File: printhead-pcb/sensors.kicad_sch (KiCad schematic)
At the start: 16 parts, among them J10 T2, J11 T3, J8 T0, J9 T1, U4 ADS1015IDGS

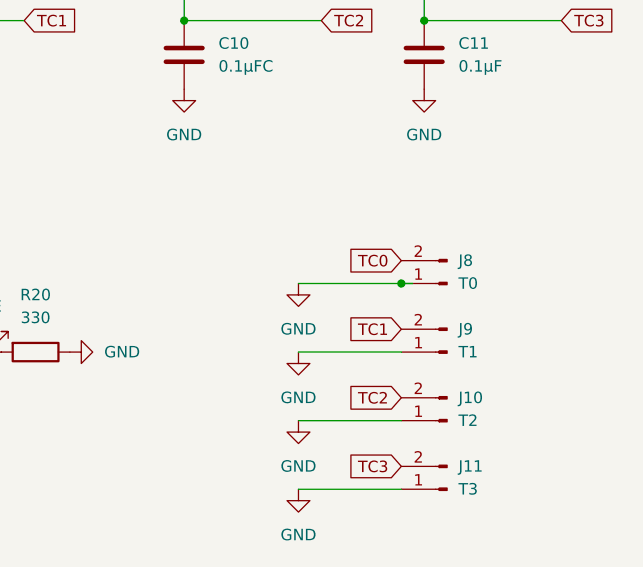
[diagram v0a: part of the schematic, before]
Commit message: removed led driver, added RJ45 (data connector), fan 3. 4. on off
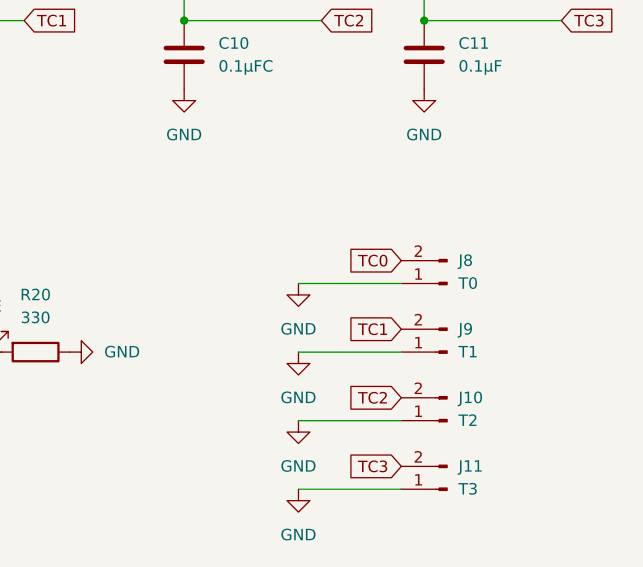
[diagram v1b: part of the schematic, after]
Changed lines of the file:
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@@
-	)
-	(junction
-		(at 176.53 125.73)
-		(diameter 0)
-		(color 0 0 0 0)
 	)
 	(junction
@@
 		(pts
 			(xy 119.38 96.52) (xy 119.38 82.55)
-		)
-		(stroke
-			(width 0)
-			(type default)
-		)
-	)
-	(wire
-		(pts
-			(xy 165.1 125.73) (xy 176.53 125.73)
 		)
 		(stroke
@@
 	(wire
 		(pts
-			(xy 177.8 125.73) (xy 176.53 125.73)
+			(xy 165.1 125.73) (xy 176.53 125.73)
 		)
 		(stroke

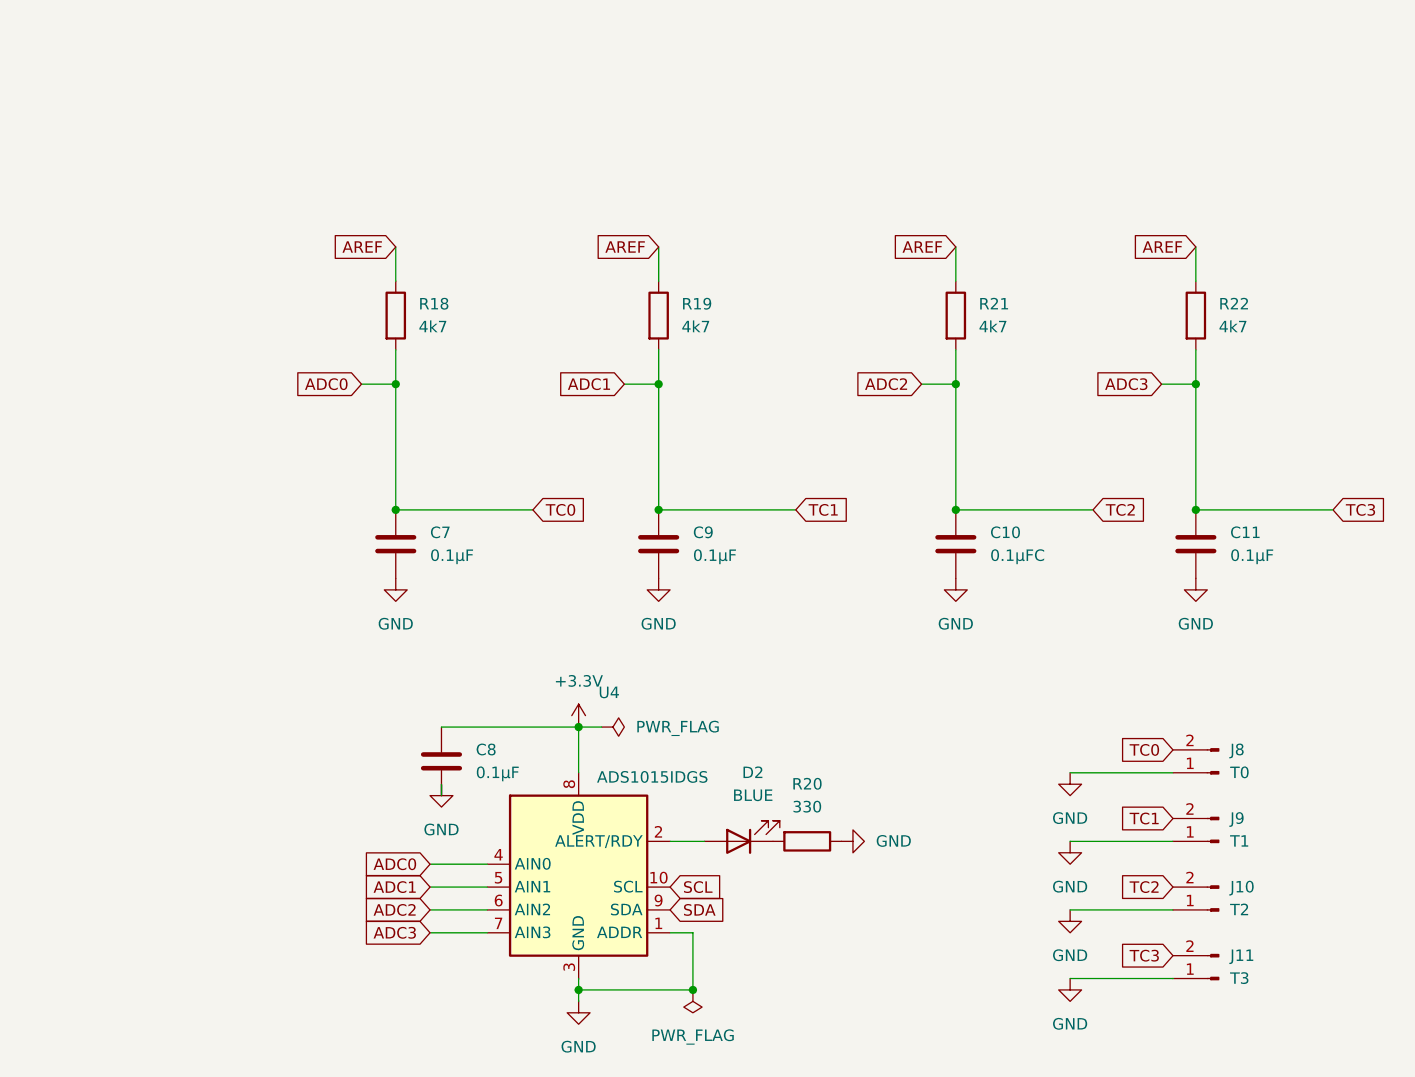
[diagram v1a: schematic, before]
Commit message: Beschriftungen im Schaltplan hinzugefügt
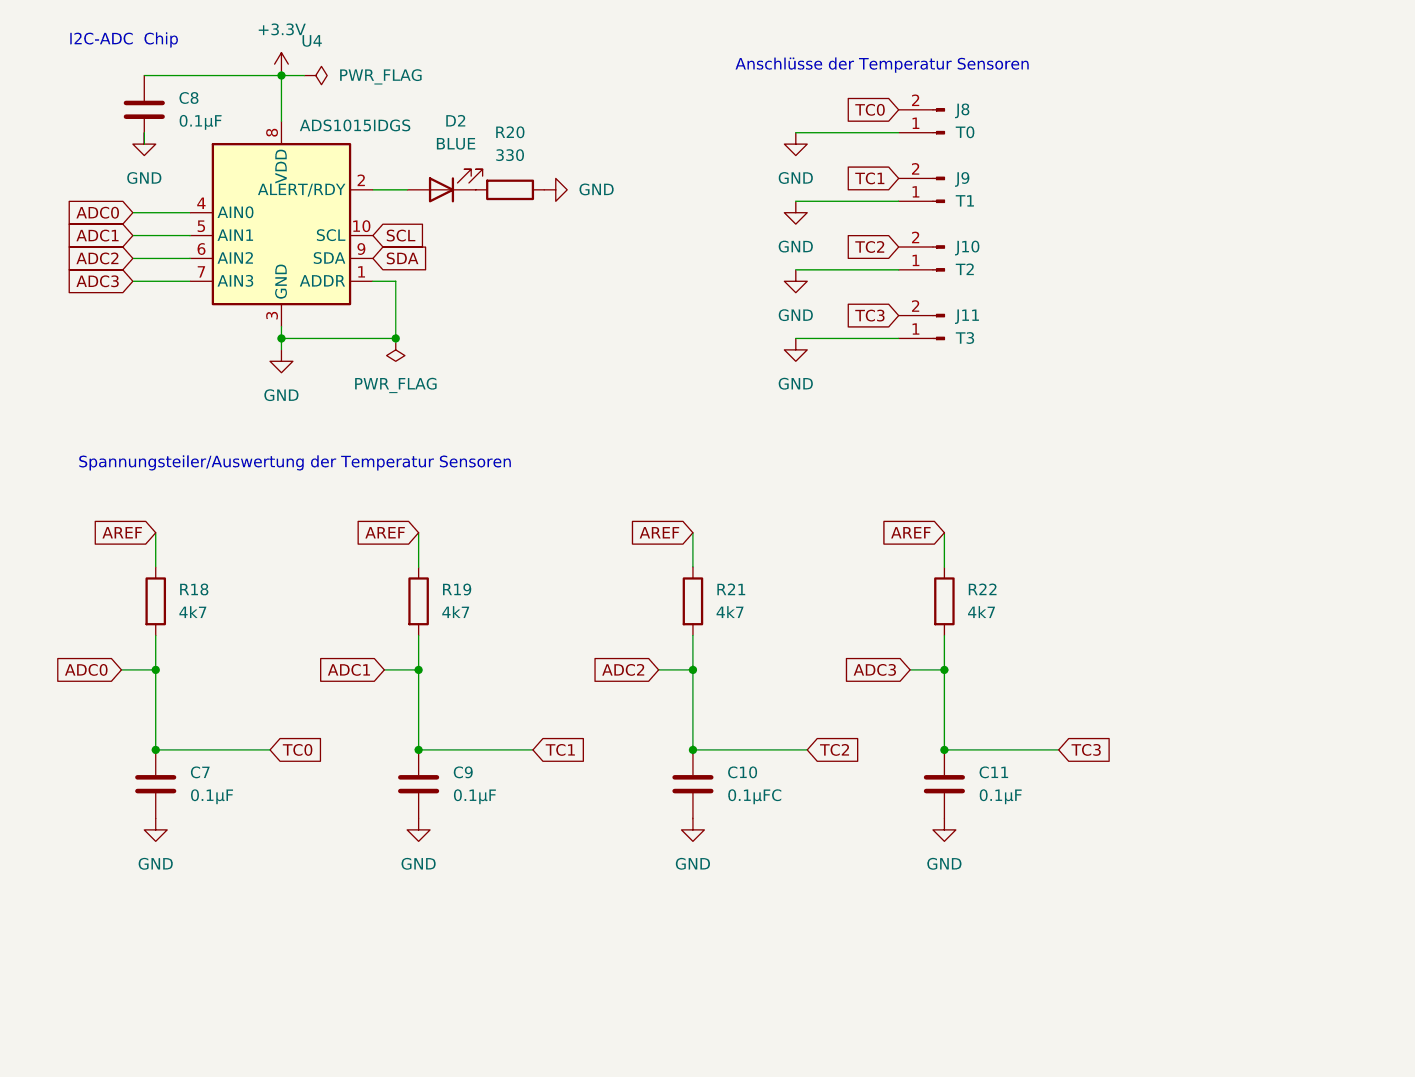
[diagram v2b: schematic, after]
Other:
- note added: "Anschlüsse der Temperatur Sensoren"
- note added: "I2C-ADC Chip"
- note added: "Spannungsteiler/Auswertung der Temperatur Sensoren"
- moved on the sheet: C10, C11, C7, C8, C9, D2, J10, J11, J8, J9, R18, R19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
